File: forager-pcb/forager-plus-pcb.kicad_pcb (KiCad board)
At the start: 2 copper layers, 114.6 x 96.3 mm, 27 parts, among them J2 Conn_01x02_Pin, U1 XIAO nRF52840 Plus

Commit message: Battery connection with silkscreen (all on one footprint)
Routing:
- net BAT: track 84.1 -> 90.2 mm
- net GND: track 855.9 -> 859.0 mm

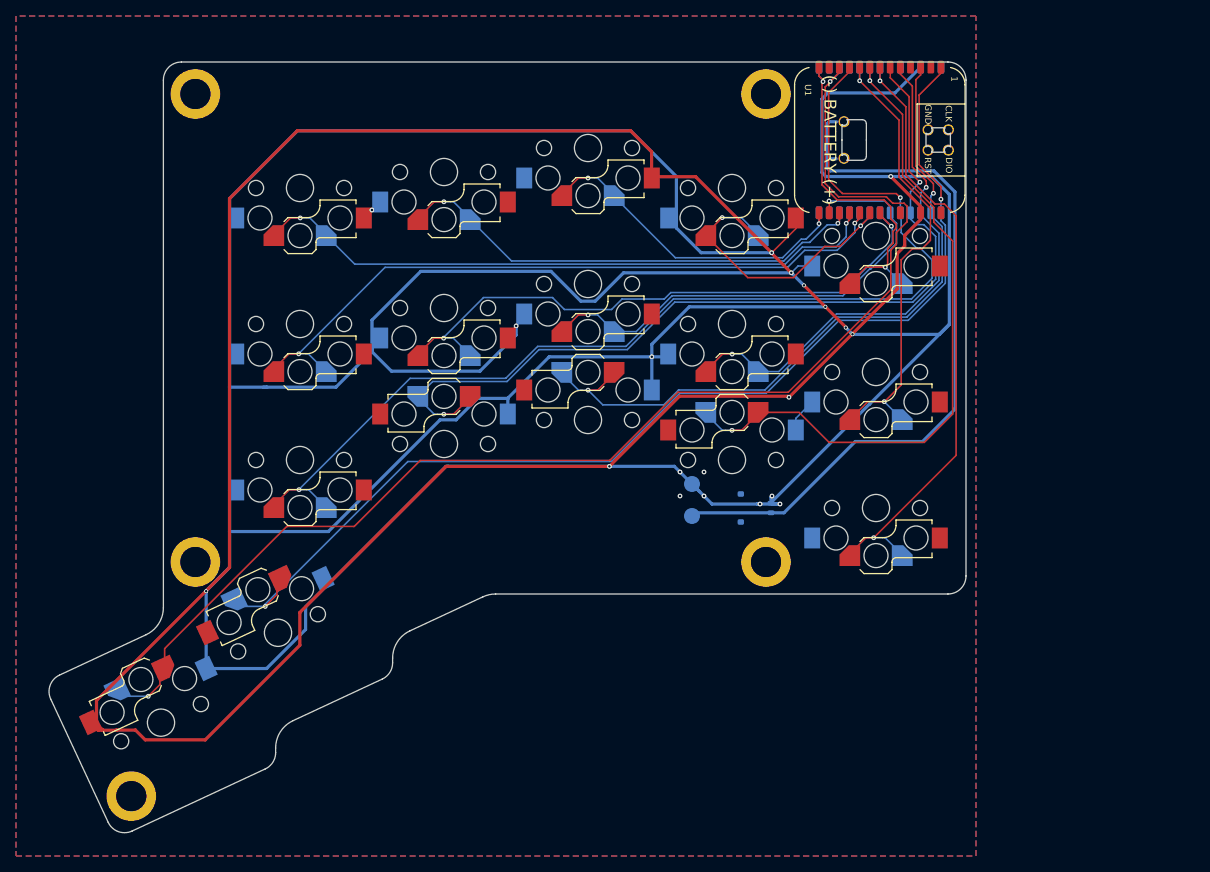
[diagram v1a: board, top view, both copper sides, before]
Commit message: Label pads D0 to D19 etc on silkscreen (one side so far)
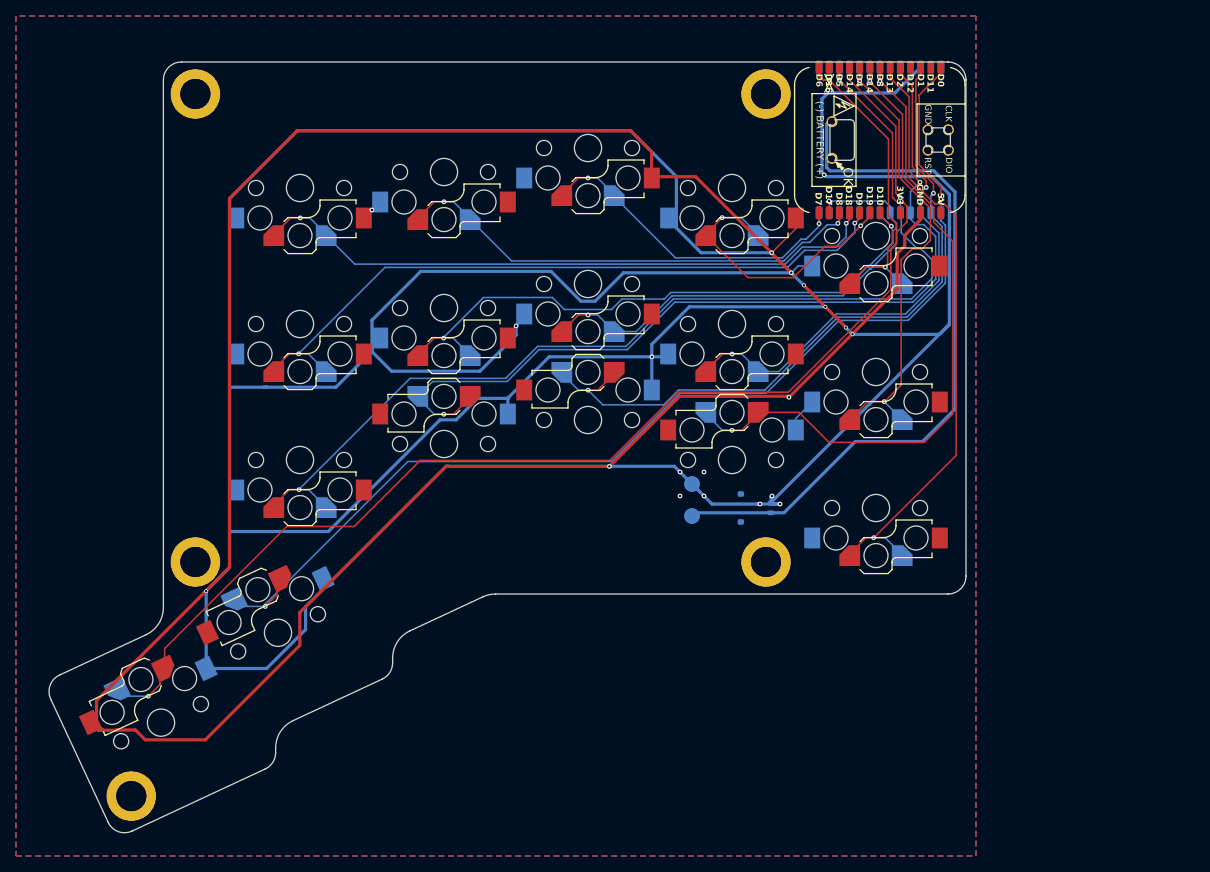
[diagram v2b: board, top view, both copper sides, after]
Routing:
- net RB0: track 134.8 -> 128.7 mm
- net RH0: track 157.4 -> 151.4 mm
- net GND: track 859.0 -> 853.7 mm
- net RT4: track 43.4 -> 40.9 mm
- net BAT: track 90.2 -> 88.1 mm

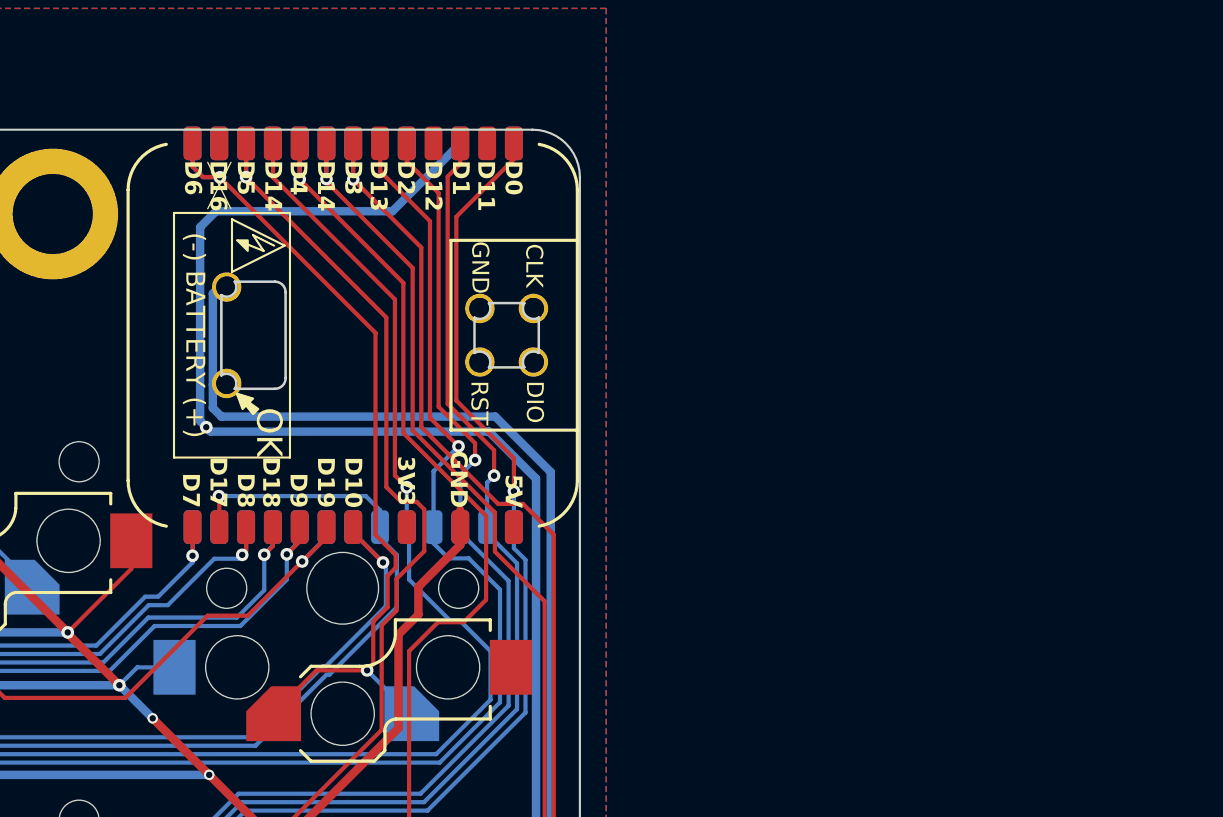
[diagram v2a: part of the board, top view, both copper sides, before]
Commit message: Combine F&B controller footprints (WIP)
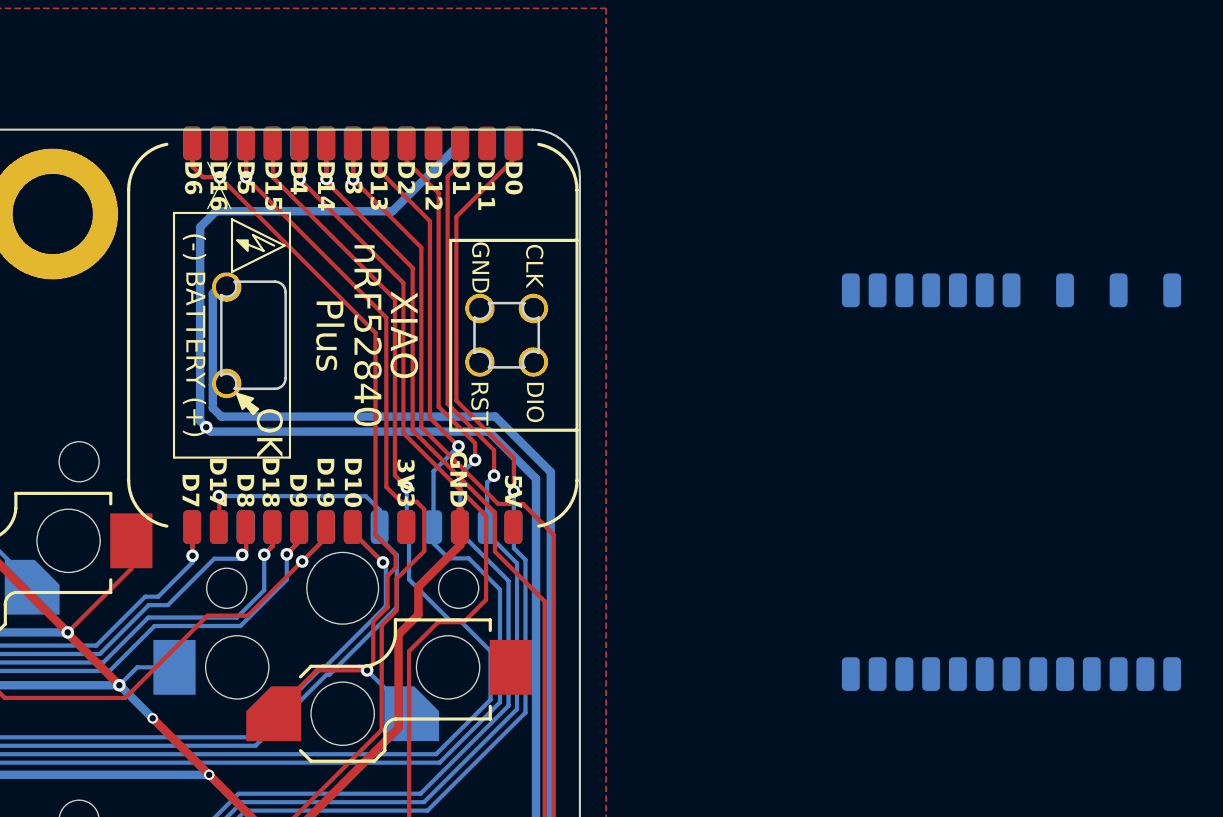
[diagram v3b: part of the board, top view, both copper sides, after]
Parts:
- moved U1 32.0 mm to (138.7, -33.0)

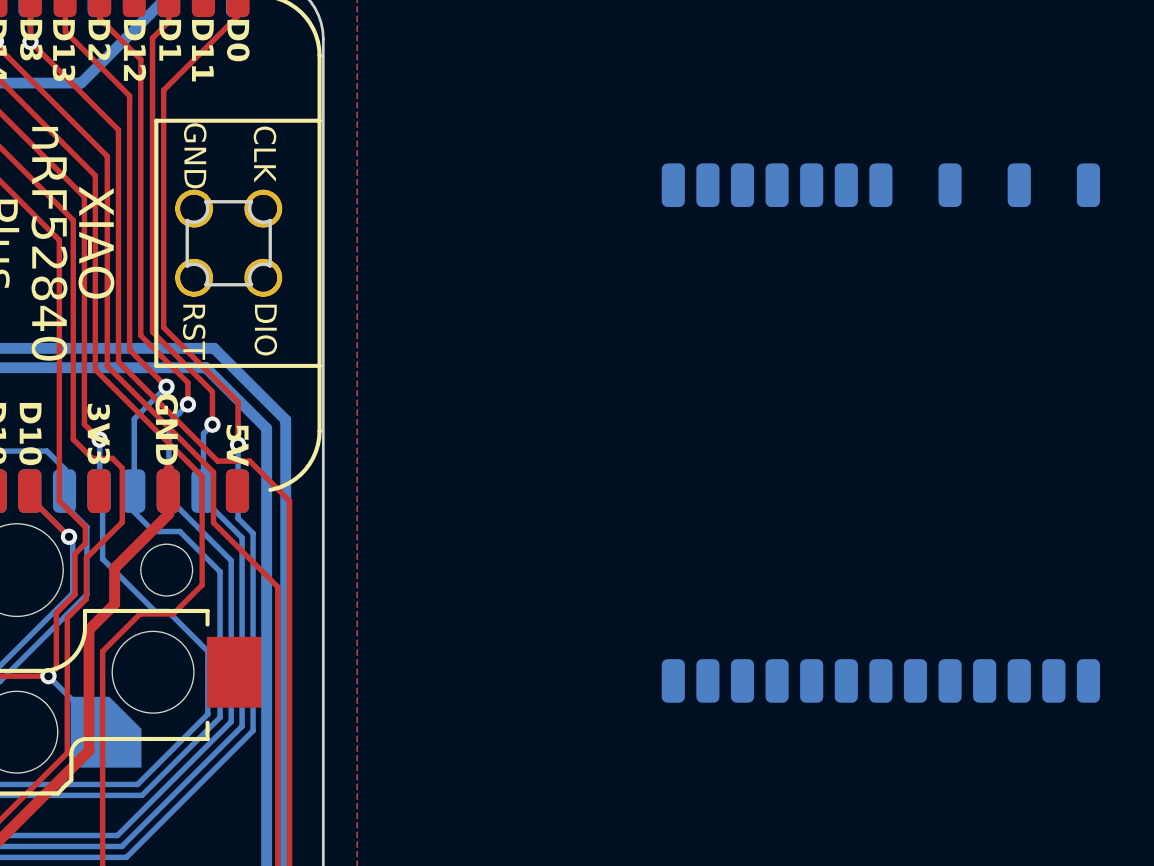
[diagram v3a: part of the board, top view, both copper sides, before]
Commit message: Combine F&B controller footprints (Still WIP)
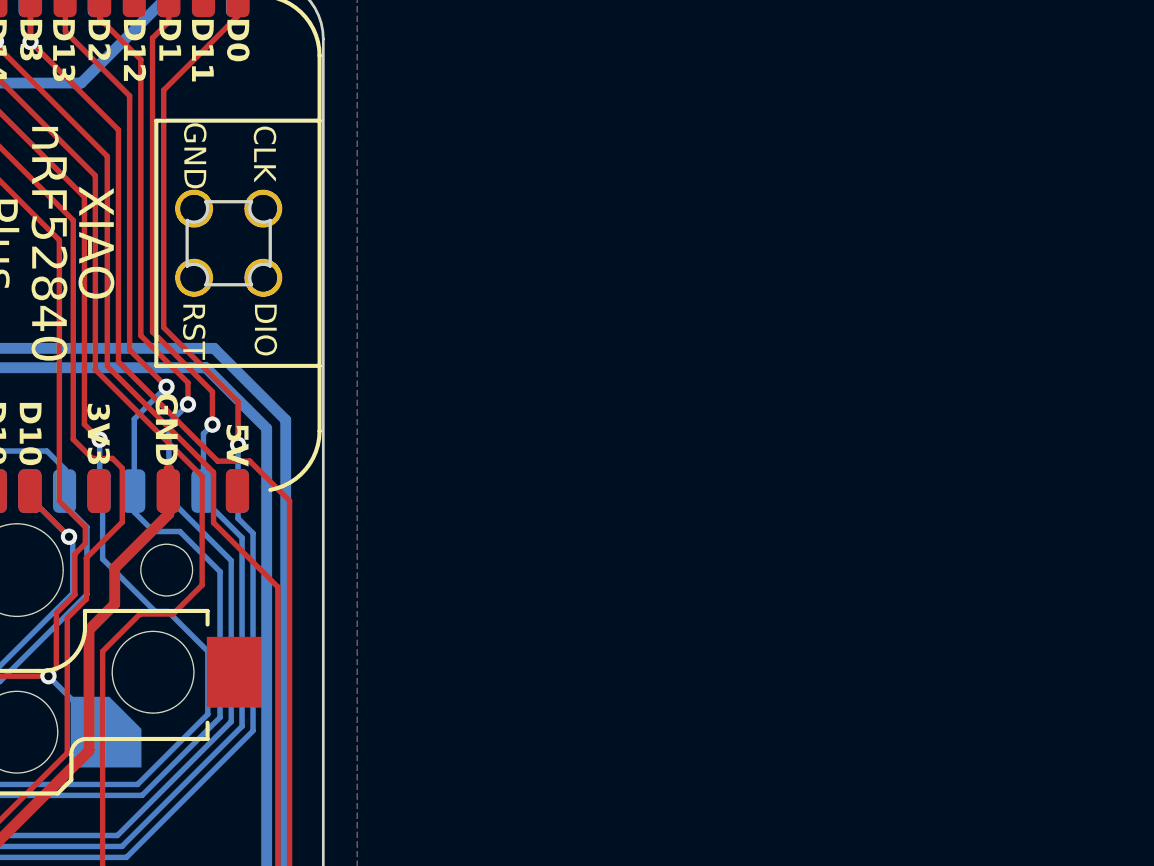
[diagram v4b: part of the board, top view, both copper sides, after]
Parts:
- removed the U1 at (138.7, -33.0)
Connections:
- U1 pad B:D0: (no net) -> RH1
- U1 pad B:D1: (no net) -> RM3
- U1 pad B:D10: (no net) -> RB4
- U1 pad B:D11: (no net) -> RB2
- U1 pad B:D12: (no net) -> RB1
- U1 pad B:D13: (no net) -> RM2
- U1 pad B:D14: (no net) -> RT3
- U1 pad B:D15: (no net) -> RT0
- U1 pad B:D19: (no net) -> RB3
- U1 pad B:D2: (no net) -> RB0
- U1 pad B:D3: (no net) -> RM1
- U1 pad B:D4: (no net) -> RM0
- U1 pad B:D5: (no net) -> RT1
- U1 pad B:D6: (no net) -> RT2
- U1 pad B:D7: (no net) -> RT4
- U1 pad B:D8: (no net) -> RH0
- U1 pad B:D9: (no net) -> RM4
- U1 pad B:GND: (no net) -> GND
- U1 pad F:3V3: (no net) -> RB0
- U1 pad F:D0: (no net) -> RH1
- U1 pad F:D1: (no net) -> RB2
- U1 pad F:D10: (no net) -> RM1
- U1 pad F:D13: (no net) -> RB1
- U1 pad F:D14: (no net) -> RB3
- U1 pad F:D15: (no net) -> RB0
- U1 pad F:D17: (no net) -> RM2
- U1 pad F:D18: (no net) -> RT0
- U1 pad F:D19: (no net) -> RT3
- U1 pad F:D2: (no net) -> RM3
- U1 pad F:D3: (no net) -> RB4
- U1 pad F:D4: (no net) -> RM4
- U1 pad F:D5: (no net) -> RH0
- U1 pad F:D6: (no net) -> RT4
- U1 pad F:D7: (no net) -> RT2
- U1 pad F:D8: (no net) -> RT1
- U1 pad F:D9: (no net) -> RM0
- U1 pad F:GND: (no net) -> GND

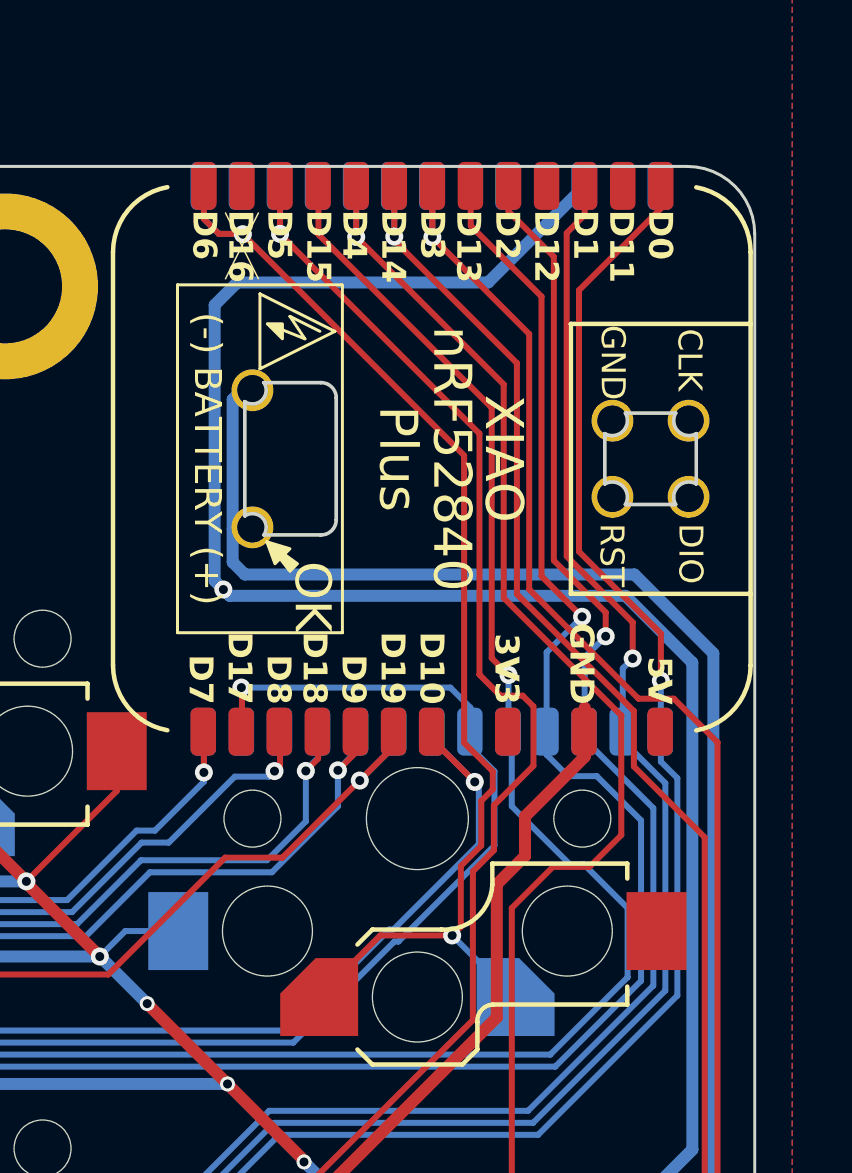
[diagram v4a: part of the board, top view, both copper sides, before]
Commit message: Fix up errors in tollerances for controller footprints
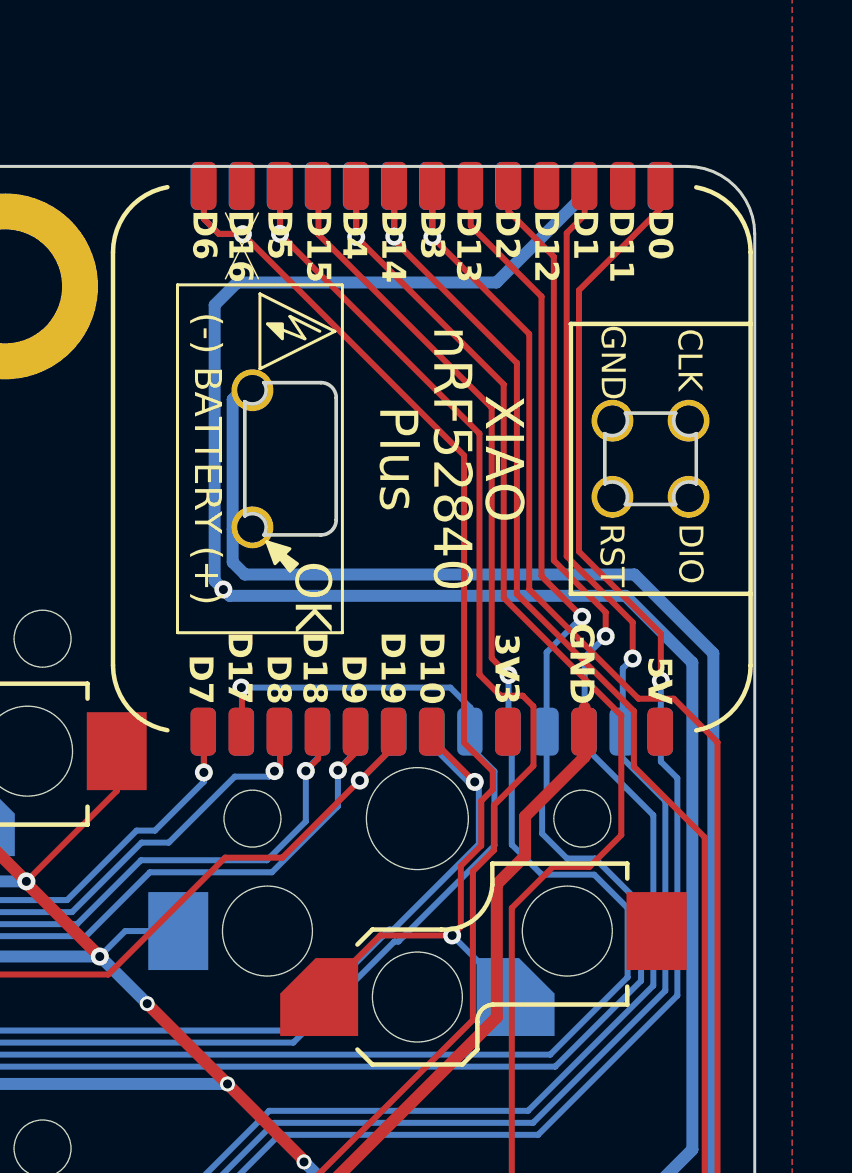
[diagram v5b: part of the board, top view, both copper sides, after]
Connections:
- U1 pad F:3V3: RB0 -> (no net)
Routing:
- net RB0: track 128.7 -> 129.4 mm
